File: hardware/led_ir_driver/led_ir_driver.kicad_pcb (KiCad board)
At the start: 2 copper layers, 70 x 40 mm, 26 parts, among them J1 MCP4725 IR 0x60, J2 PI I2C INPUT / IR OUT, J3 MCP4725 RED 0x61, J4 RED DAC OUT / GND, J5 IR LED A / K, J6 RED LED A / K, J7 5V INPUT / GND, Q1 2N4401 / E-B-C, Q2 2N4401 / E-B-C, U1 LM358P / DIP8 socket

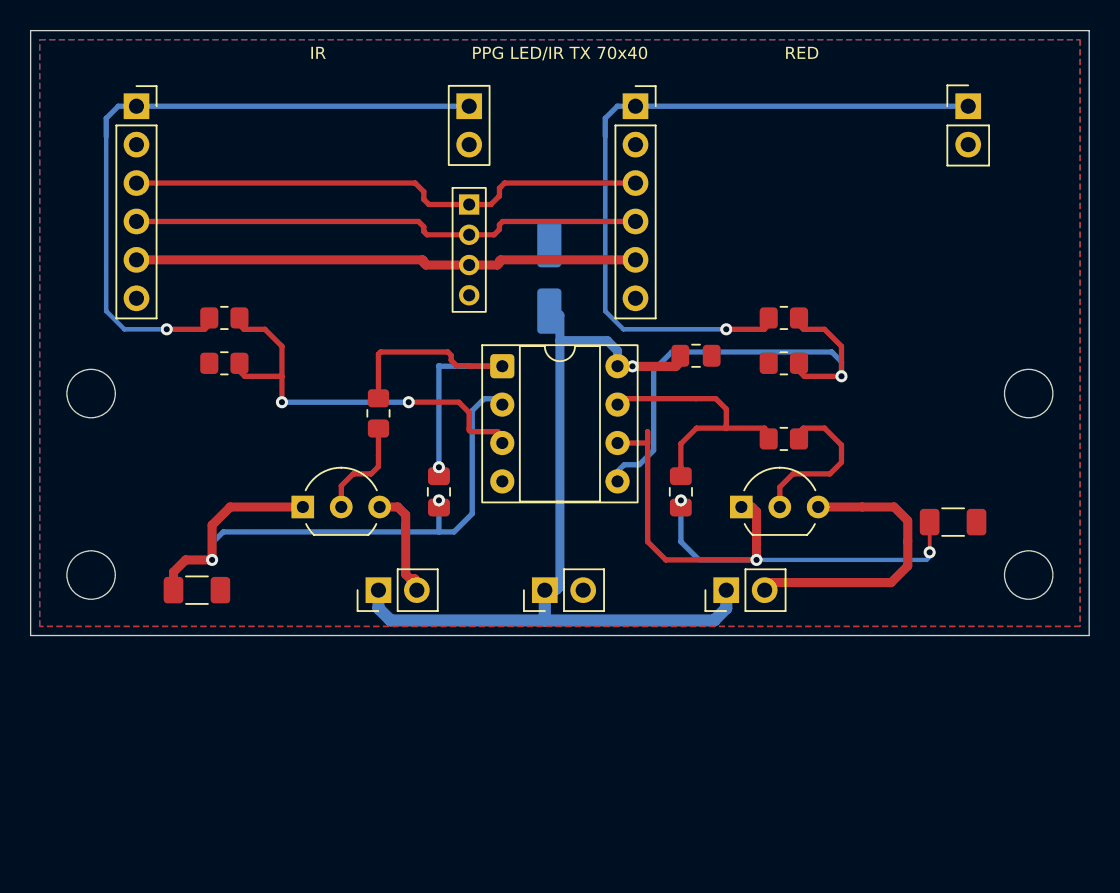
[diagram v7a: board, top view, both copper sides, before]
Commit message: Update README.md, hardware 45-degree routing and OPT101 diagnostic docs
- Fix version line in README.md to ensure version consistency test passes
- Document persistent live A0/A2 RX monitor dock and touch UI scaling
- Document OPT101 physical bench diagnostic protocol (docs/opt101-a0-diagnostic-2026-10-01.md)
- Detail 45-degree chamfered PCB routing, segment cleanup, and updated wiring guides
- Update repository tree and refreshed manufacturing release ZIPs
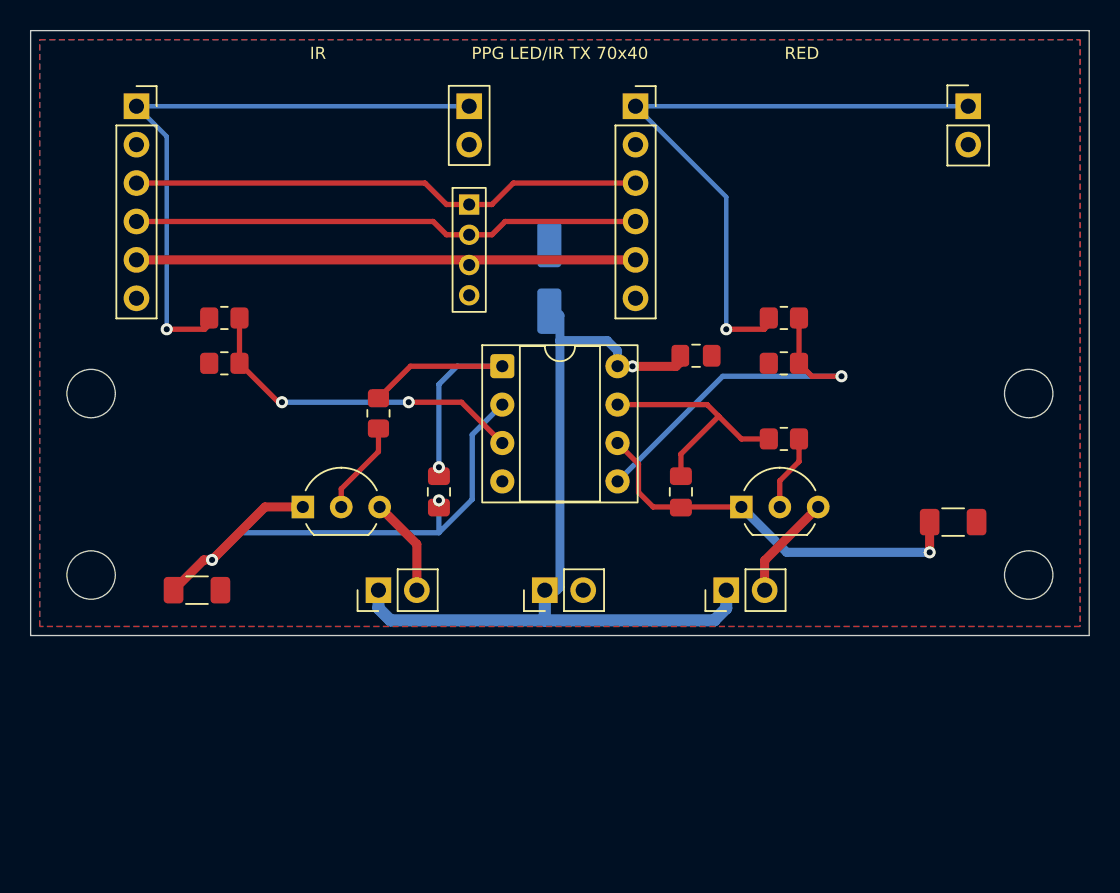
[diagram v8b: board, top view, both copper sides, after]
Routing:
- net /SENSE_RED: track 44.6 -> 26.7 mm, vias 3 -> 1
- net /LED_K_RED: track 19.6 -> 6.97 mm
- net /CMD_RED: track 32.4 -> 23.9 mm
- net /DAC_RED: track 49.0 -> 42.6 mm
- net /BASE_RED: track 11.0 -> 5.03 mm
- net /CMD_IR: track 27.6 -> 22.6 mm
- net /SENSE_IR: track 43.7 -> 39.4 mm
- net /DAC_IR: track 45.0 -> 41.0 mm
- net /AMP_IR: track 23.3 -> 19.8 mm
- net /AMP_RED: track 17.7 -> 15.9 mm
- net /LED_K_IR: track 7.40 -> 6.52 mm
- net /BASE_IR: track 6.90 -> 6.21 mm
- net /SCL: track 34.8 -> 34.2 mm
